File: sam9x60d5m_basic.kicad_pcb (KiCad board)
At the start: 2 copper layers, 3 parts, among them U1 ME6211C33M5, U2 VRH1202LT, U3 NUC980DR61Y

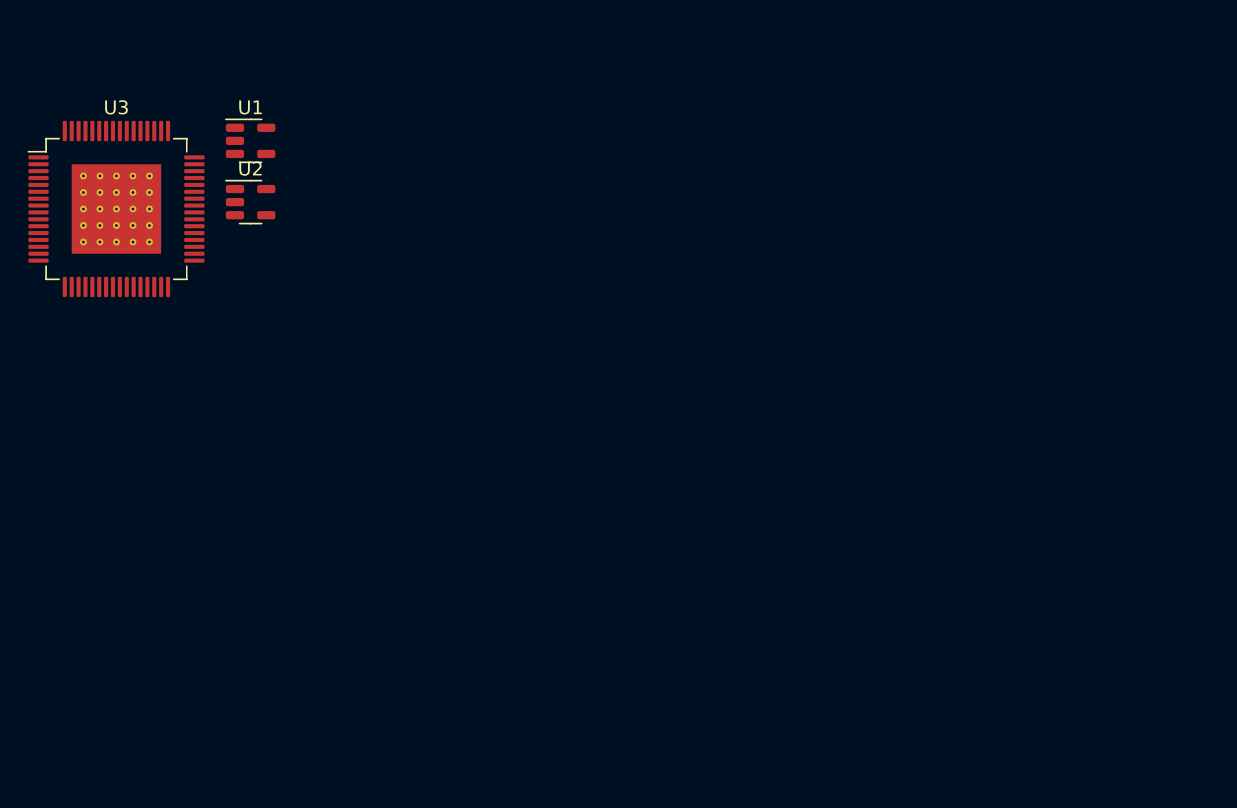
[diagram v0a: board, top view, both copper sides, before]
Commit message: Finish buck converters; include custom symbols and footprints
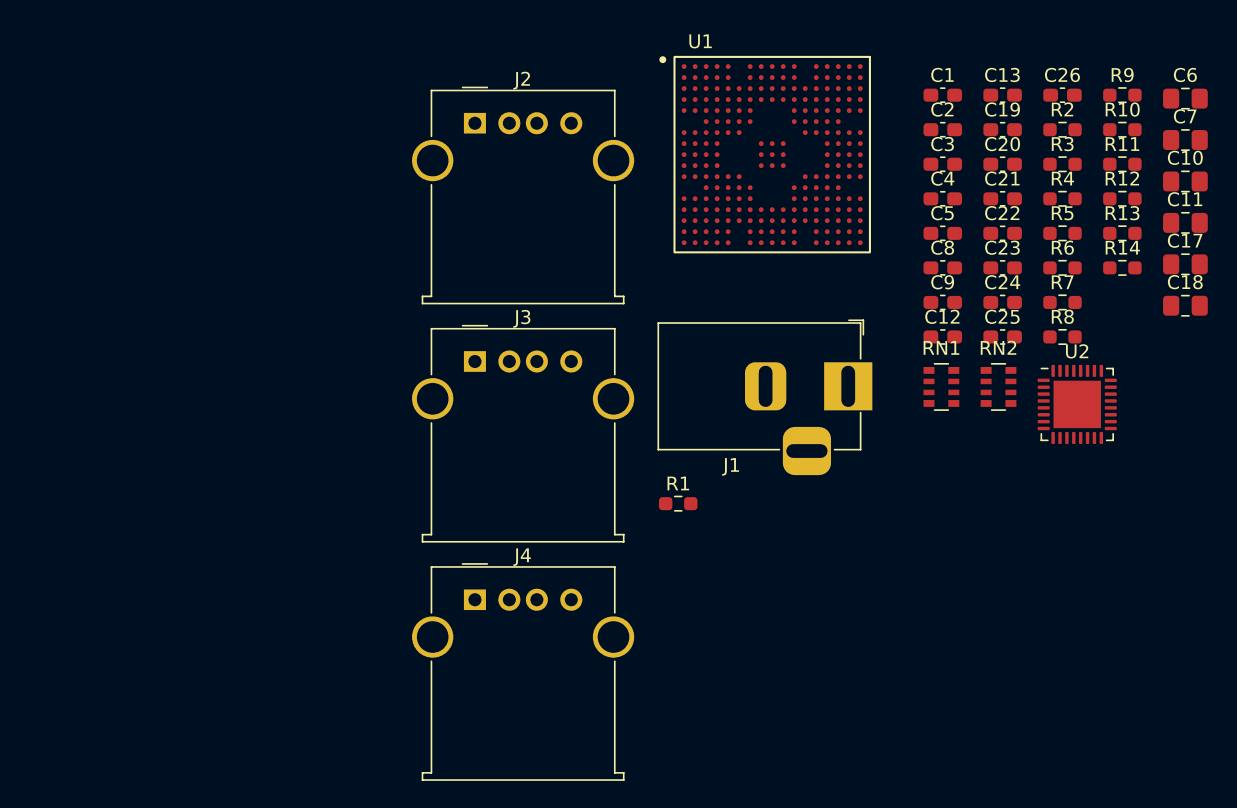
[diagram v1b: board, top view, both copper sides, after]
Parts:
- removed U3: NUC980DR61Y, Package_QFP:LQFP-64-1EP_10x10mm_P0.5mm_EP6.5x6.5mm_ThermalVias
- added C1: 47n, Capacitor_SMD:C_0603_1608Metric_Pad1.08x0.95mm_HandSolder, F.Cu at (178.7, 67.5)
- added C10: 22u, Capacitor_SMD:C_0805_2012Metric_Pad1.18x1.45mm_HandSolder, F.Cu at (196.3, 73.8)
- added C11: 22u, Capacitor_SMD:C_0805_2012Metric_Pad1.18x1.45mm_HandSolder, F.Cu at (196.3, 76.8)
- added C12: 22p, Capacitor_SMD:C_0603_1608Metric_Pad1.08x0.95mm_HandSolder, F.Cu at (178.7, 85.0)
- added C13: 47n, Capacitor_SMD:C_0603_1608Metric_Pad1.08x0.95mm_HandSolder, F.Cu at (183.0, 67.5)
- added C17: 22u, Capacitor_SMD:C_0805_2012Metric_Pad1.18x1.45mm_HandSolder, F.Cu at (196.3, 79.8)
- added C18: 22u, Capacitor_SMD:C_0805_2012Metric_Pad1.18x1.45mm_HandSolder, F.Cu at (196.3, 82.8)
- added C19: 680p, Capacitor_SMD:C_0603_1608Metric_Pad1.08x0.95mm_HandSolder, F.Cu at (183.0, 70.0)
- added C2: 1u, Capacitor_SMD:C_0603_1608Metric_Pad1.08x0.95mm_HandSolder, F.Cu at (178.7, 70.0)
- added C20: 1n, Capacitor_SMD:C_0603_1608Metric_Pad1.08x0.95mm_HandSolder, F.Cu at (183.0, 72.5)
- added C21: 1n8, Capacitor_SMD:C_0603_1608Metric_Pad1.08x0.95mm_HandSolder, F.Cu at (183.0, 75.0)
- added C22: 10n, Capacitor_SMD:C_0603_1608Metric_Pad1.08x0.95mm_HandSolder, F.Cu at (183.0, 77.5)
- added C23: 10n, Capacitor_SMD:C_0603_1608Metric_Pad1.08x0.95mm_HandSolder, F.Cu at (183.0, 80.0)
- added C24: 10n, Capacitor_SMD:C_0603_1608Metric_Pad1.08x0.95mm_HandSolder, F.Cu at (183.0, 82.5)
- added C25: 1u, Capacitor_SMD:C_0603_1608Metric_Pad1.08x0.95mm_HandSolder, F.Cu at (183.0, 85.0)
- added C26: 22p, Capacitor_SMD:C_0603_1608Metric_Pad1.08x0.95mm_HandSolder, F.Cu at (187.4, 67.5)
- added C3: 10u, Capacitor_SMD:C_0603_1608Metric_Pad1.08x0.95mm_HandSolder, F.Cu at (178.7, 72.5)
- added C4: 10u, Capacitor_SMD:C_0603_1608Metric_Pad1.08x0.95mm_HandSolder, F.Cu at (178.7, 75.0)
- added C5: 10u, Capacitor_SMD:C_0603_1608Metric_Pad1.08x0.95mm_HandSolder, F.Cu at (178.7, 77.5)
- added C6: 22u, Capacitor_SMD:C_0805_2012Metric_Pad1.18x1.45mm_HandSolder, F.Cu at (196.3, 67.7)
- added C7: 22u, Capacitor_SMD:C_0805_2012Metric_Pad1.18x1.45mm_HandSolder, F.Cu at (196.3, 70.7)
- added C8: 22p, Capacitor_SMD:C_0603_1608Metric_Pad1.08x0.95mm_HandSolder, F.Cu at (178.7, 80.0)
- added C9: 47n, Capacitor_SMD:C_0603_1608Metric_Pad1.08x0.95mm_HandSolder, F.Cu at (178.7, 82.5)
- added J1: Barrel_Jack_Switch, Connector_BarrelJack:BarrelJack_Horizontal, F.Cu at (171.8, 88.6)
- added J2: USB_A, Connector_USB:USB_A_Molex_67643_Horizontal, F.Cu at (144.7, 69.5)
- added J3: USB_A, Connector_USB:USB_A_Molex_67643_Horizontal, F.Cu at (144.7, 86.8)
- added J4: USB_A, Connector_USB:USB_A_Molex_67643_Horizontal, F.Cu at (144.7, 104.1)
- added R1: 5k62 ±1%, Resistor_SMD:R_0603_1608Metric_Pad0.98x0.95mm_HandSolder, F.Cu at (159.5, 97.2)
- added R10: 18k, Resistor_SMD:R_0603_1608Metric_Pad0.98x0.95mm_HandSolder, F.Cu at (191.7, 70.0)
- added R11: 20k, Resistor_SMD:R_0603_1608Metric_Pad0.98x0.95mm_HandSolder, F.Cu at (191.7, 72.5)
- added R12: 20k, Resistor_SMD:R_0603_1608Metric_Pad0.98x0.95mm_HandSolder, F.Cu at (191.7, 75.0)
- added R13: 56k, Resistor_SMD:R_0603_1608Metric_Pad0.98x0.95mm_HandSolder, F.Cu at (191.7, 77.5)
- added R14: 100k, Resistor_SMD:R_0603_1608Metric_Pad0.98x0.95mm_HandSolder, F.Cu at (191.7, 80.0)
- added R2: 27k, Resistor_SMD:R_0603_1608Metric_Pad0.98x0.95mm_HandSolder, F.Cu at (187.4, 70.0)
- added R3: 39k, Resistor_SMD:R_0603_1608Metric_Pad0.98x0.95mm_HandSolder, F.Cu at (187.4, 72.5)
- added R4: 8k67, Resistor_SMD:R_0603_1608Metric_Pad0.98x0.95mm_HandSolder, F.Cu at (187.4, 75.0)
- added R5: 10k, Resistor_SMD:R_0603_1608Metric_Pad0.98x0.95mm_HandSolder, F.Cu at (187.4, 77.5)
- added R6: 39k, Resistor_SMD:R_0603_1608Metric_Pad0.98x0.95mm_HandSolder, F.Cu at (187.4, 80.0)
- added R7: 19k5, Resistor_SMD:R_0603_1608Metric_Pad0.98x0.95mm_HandSolder, F.Cu at (187.4, 82.5)
- added R8: 56k, Resistor_SMD:R_0603_1608Metric_Pad0.98x0.95mm_HandSolder, F.Cu at (187.4, 85.0)
- added R9: 33k, Resistor_SMD:R_0603_1608Metric_Pad0.98x0.95mm_HandSolder, F.Cu at (191.7, 67.5)
- added RN1: 22k, Resistor_SMD:R_Array_Convex_4x0603, F.Cu at (178.6, 88.7)
- added RN2: 10k, Resistor_SMD:R_Array_Convex_4x0603, F.Cu at (182.7, 88.7)
- U1: value ME6211C33M5 -> SAM9X60D; footprint Package_TO_SOT_SMD:SOT-23-5 -> SAM9X60D:BGA-233_14x14mm_Layout17x17_P0.8mm_Ball0.4mm
- U2: value VRH1202LT -> TPS65261; footprint Package_TO_SOT_SMD:SOT-23-5 -> Package_DFN_QFN:QFN-32-1EP_5x5mm_P0.5mm_EP3.45x3.45mm
- moved U2 61.8 mm to (188.5, 90.0)
- moved U1 37.9 mm to (166.3, 71.8)
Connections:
- U2 pad 1: +5V -> Net-(RN1-R1.1)
- U2 pad 2: GND -> /Power/RESET_OUT
- U2 pad 3: +5V -> /Power/RESET_OUT
- U2 pad 4: (no net) -> Net-(RN1-R4.1)
- U2 pad 5: +1V2 -> Net-(U2-V7V)
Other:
- copper layers 2 -> 4
- rule pad_to_mask_clearance: 0 -> 0.038
